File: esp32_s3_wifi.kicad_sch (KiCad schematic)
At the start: 1 part, among them U8 ESP32-S3-WROOM-1

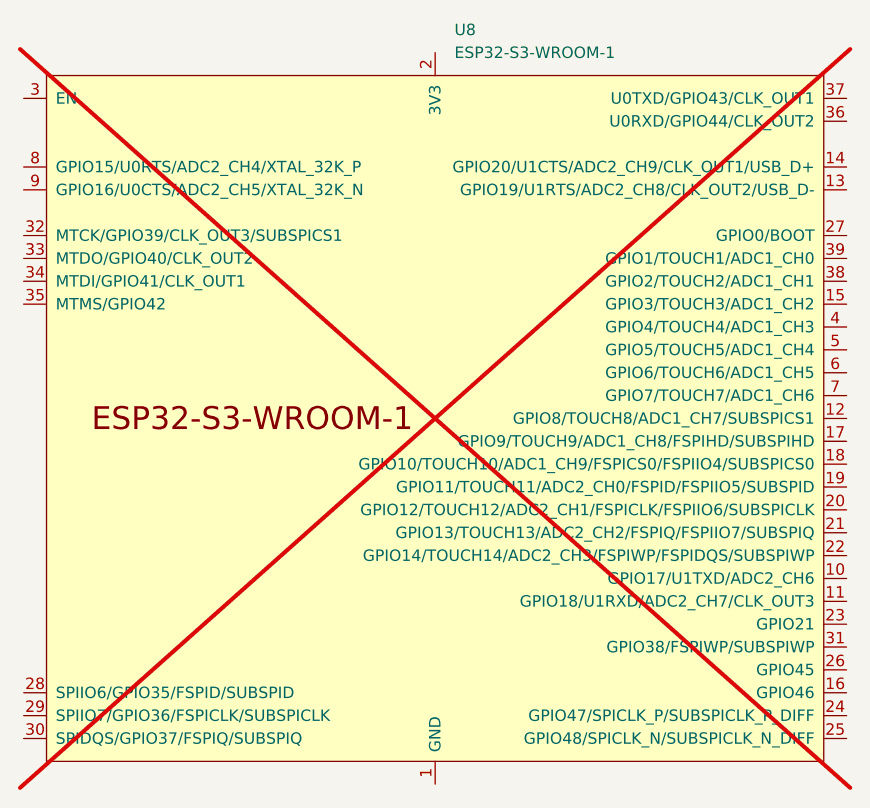
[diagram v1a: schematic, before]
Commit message: mark all extra pins as no-connect. erc fixed.
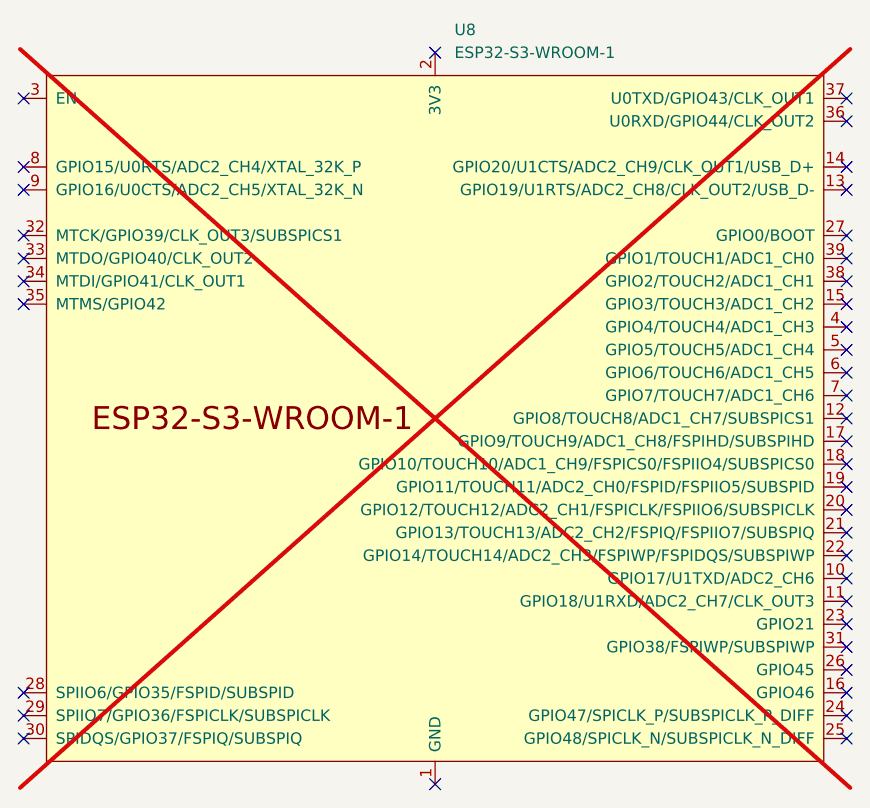
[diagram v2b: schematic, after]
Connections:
- no-connect marks 0 -> 39
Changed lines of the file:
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@@
 	(generator_version "10.0")
 	(paper "A4")
+	(no_connect
+		(at 190.5 123.19)
+	)
+	(no_connect
+		(at 99.06 77.47)
+	)
+	(no_connect
+		(at 190.5 120.65)
+	)
+	(no_connect
+		(at 190.5 105.41)
+	)
+	(no_connect
+		(at 99.06 62.23)
+	)
+	(no_connect
+		(at 144.78 138.43)
+	)
+	(no_connect
+		(at 190.5 95.25)
+	)
+	(no_connect
+		(at 190.5 72.39)
+	)
+	(no_connect
+		(at 99.06 128.27)
+	)
+	(no_connect
+		(at 190.5 100.33)
+	)
+	(no_connect
+		(at 190.5 115.57)
+	)
+	(no_connect
+		(at 190.5 77.47)
+	)
+	(no_connect
+		(at 190.5 85.09)
+	)
+	(no_connect
+		(at 190.5 90.17)
+	)
+	(no_connect
+		(at 99.06 69.85)
+	)
+	(no_connect
+		(at 190.5 97.79)
+	)
+	(no_connect
+		(at 99.06 72.39)
+	)
+	(no_connect
+		(at 190.5 130.81)
+	)
+	(no_connect
+		(at 190.5 133.35)
+	)
+	(no_connect
+		(at 190.5 102.87)
+	)
+	(no_connect
+		(at 190.5 80.01)
+	)
+	(no_connect
+		(at 144.78 57.15)
+	)
+	(no_connect
+		(at 190.5 92.71)
+	)
+	(no_connect
+		(at 99.06 133.35)
+	)
+	(no_connect
+		(at 190.5 125.73)
+	)
+	(no_connect
+		(at 190.5 69.85)
+	)
+	(no_connect
+		(at 190.5 64.77)
+	)
+	(no_connect
+		(at 190.5 110.49)
+	)
+	(no_connect
+		(at 190.5 62.23)
+	)
+	(no_connect
+		(at 99.06 85.09)
+	)
+	(no_connect
+		(at 99.06 130.81)
+	)
+	(no_connect
+		(at 99.06 82.55)
+	)
+	(no_connect
+		(at 190.5 87.63)
+	)
+	(no_connect
+		(at 190.5 118.11)
+	)
+	(no_connect
+		(at 99.06 80.01)
+	)
+	(no_connect
+		(at 190.5 82.55)
+	)
+	(no_connect
+		(at 190.5 107.95)
+	)
+	(no_connect
+		(at 190.5 113.03)
+	)
+	(no_connect
+		(at 190.5 128.27)
+	)
 	(symbol
 		(lib_id "esp32:ESP32-S3-WROOM-1")

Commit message: update parts for 22uf/1uf. Update footprint for RP* items
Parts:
- U8: Digikey (none) -> 5407-ESP32-S3-WROOM-1-N16R8CT-ND; MPN (none) -> 356-ESP32S3WRM1N16R8
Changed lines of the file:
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@@
+			)
+		)
+		(property "Arrow" ""
+			(at 144.78 97.79 0)
+			(hide yes)
+			(show_name no)
+			(do_not_autoplace no)
+			(effects
+				(font
+					(size 1.524 1.524)
+				)
+			)
+		)
+		(property "DatasheetLC" ""
+			(at 144.78 97.79 0)
+			(hide yes)
+			(show_name no)
+			(do_not_autoplace no)
+			(effects
+				(font
+					(size 1.524 1.524)
+				)
+			)
+		)
+		(property "LCS_C2" ""
+			(at 144.78 97.79 0)
+			(hide yes)
+			(show_name no)
+			(do_not_autoplace no)
+			(effects
+				(font
+					(size 1.524 1.524)
+				)
+			)
+		)
+		(property "MP_N4" ""
+			(at 144.78 97.79 0)
+			(hide yes)
+			(show_name no)
+			(do_not_autoplace no)
+			(effects
+				(font
+					(size 1.524 1.524)
+				)
+			)
+		)
+		(property "MP_N5" ""
+			(at 144.78 97.79 0)
+			(hide yes)
+			(show_name no)
+			(do_not_autoplace no)
+			(effects
+				(font
+					(size 1.524 1.524)
+				)
+			)
+		)
+		(property "Vertical" ""
+			(at 144.78 97.79 0)
+			(hide yes)
+			(show_name no)
+			(do_not_autoplace no)
+			(effects
+				(font
+					(size 1.524 1.524)
+				)
+			)
+		)
+		(property "price100_Mouser" ""
+			(at 144.78 97.79 0)
+			(hide yes)
+			(show_name no)
+			(do_not_autoplace no)
+			(effects
+				(font
+					(size 1.524 1.524)
+				)
+			)
+		)
+		(property "price1200_Chip1stop" ""
+			(at 144.78 97.79 0)
+			(hide yes)
+			(show_name no)
+			(do_not_autoplace no)
+			(effects
+				(font
+					(size 1.524 1.524)
+				)
+			)
+		)
+		(property "price300_LCSC" ""
+			(at 144.78 97.79 0)
+			(hide yes)
+			(show_name no)
+			(do_not_autoplace no)
+			(effects
+				(font
+					(size 1.524 1.524)
+				)
+			)
+		)
+		(property "price300_Vertical" ""
+			(at 144.78 97.79 0)
+			(hide yes)
+			(show_name no)
+			(do_not_autoplace no)
+			(effects
+				(font
+					(size 1.524 1.524)
+				)
+			)
+		)
+		(property "price_Arrow" ""
+			(at 144.78 97.79 0)
+			(hide yes)
+			(show_name no)
+			(do_not_autoplace no)
+			(effects
+				(font
+					(size 1.524 1.524)
+				)
+			)
+		)
+		(property "Digikey" "5407-ESP32-S3-WROOM-1-N16R8CT-ND"
+			(at 144.78 97.79 0)
+			(hide yes)
+			(show_name no)
+			(do_not_autoplace no)
+			(effects
+				(font
+					(size 1.524 1.524)
+				)
+			)
+		)
+		(property "MPN" "356-ESP32S3WRM1N16R8"
+			(at 144.78 97.79 0)
+			(hide yes)
+			(show_name no)
+			(do_not_autoplace no)
+			(effects
+				(font
+					(size 1.524 1.524)
+				)
 			)
 		)
